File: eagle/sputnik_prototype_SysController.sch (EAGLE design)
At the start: 50 parts, among them U1 MEGA128-M, Y2 8MHZ

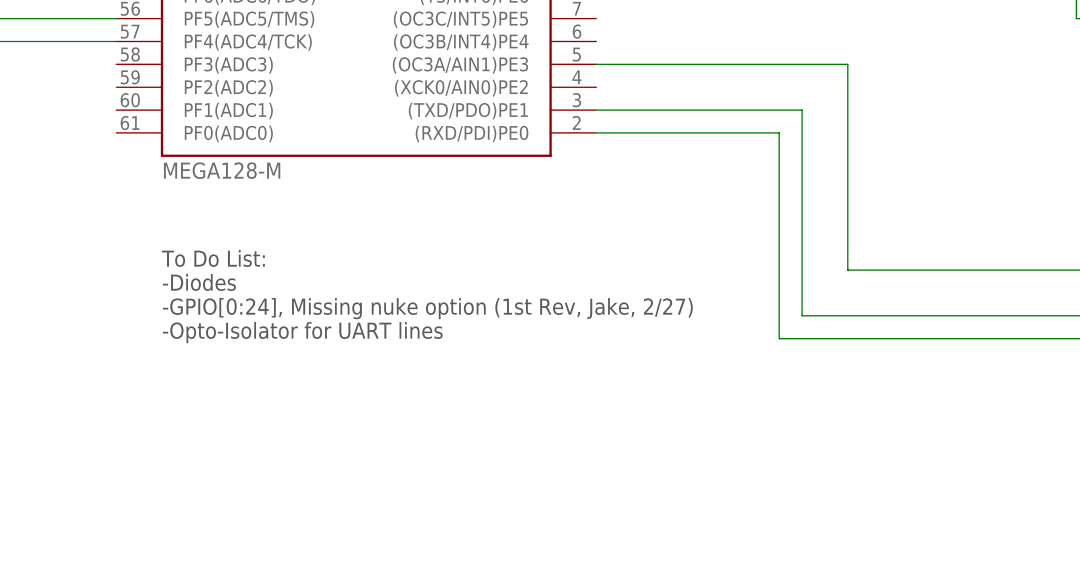
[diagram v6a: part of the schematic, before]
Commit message: Updated to do lists
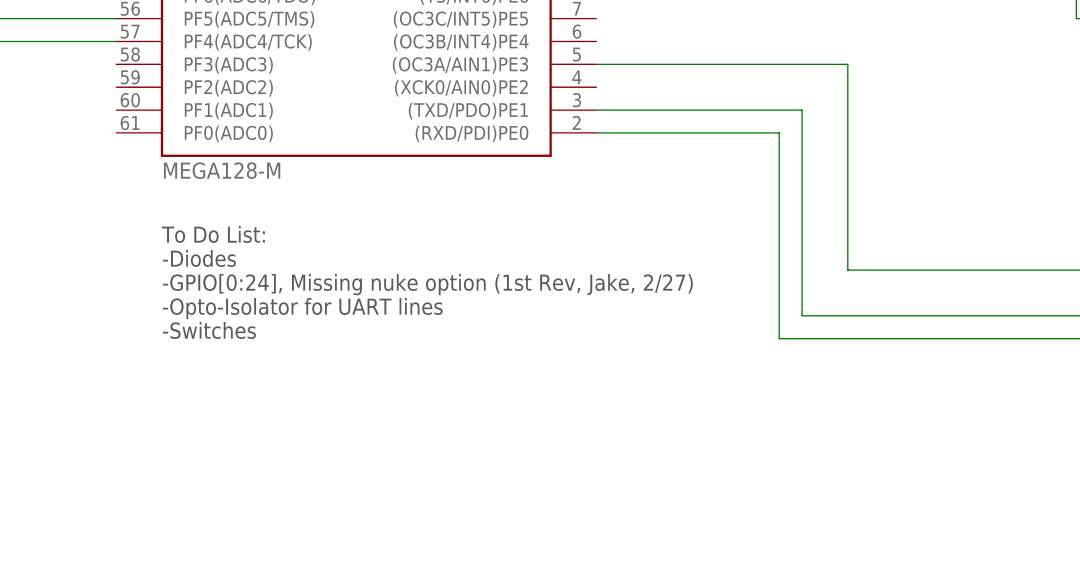
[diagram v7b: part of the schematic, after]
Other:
- note added: "To Do List: -Diodes -GPIO[0:24], Missing nuke option (1st Rev, Jake, 2/27) -Opto-Isolator for UART lines -Switches"
- note removed: "To Do List: -Diodes -GPIO[0:24], Missing nuke option (1st Rev, Jake, 2/27) -Opto-Isolator for UART lines"
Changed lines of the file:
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@@
 -Diodes
 -GPIO[0:24], Missing nuke option (1st Rev, Jake, 2/27)
--Opto-Isolator for UART lines</text>
+-Opto-Isolator for UART lines
+-Switches</text>
 <text x="431.8" y="287.02" size="1.778" layer="97">GPIO</text>
 <text x="431.8" y="248.92" size="1.778" layer="97">GPIO</text>

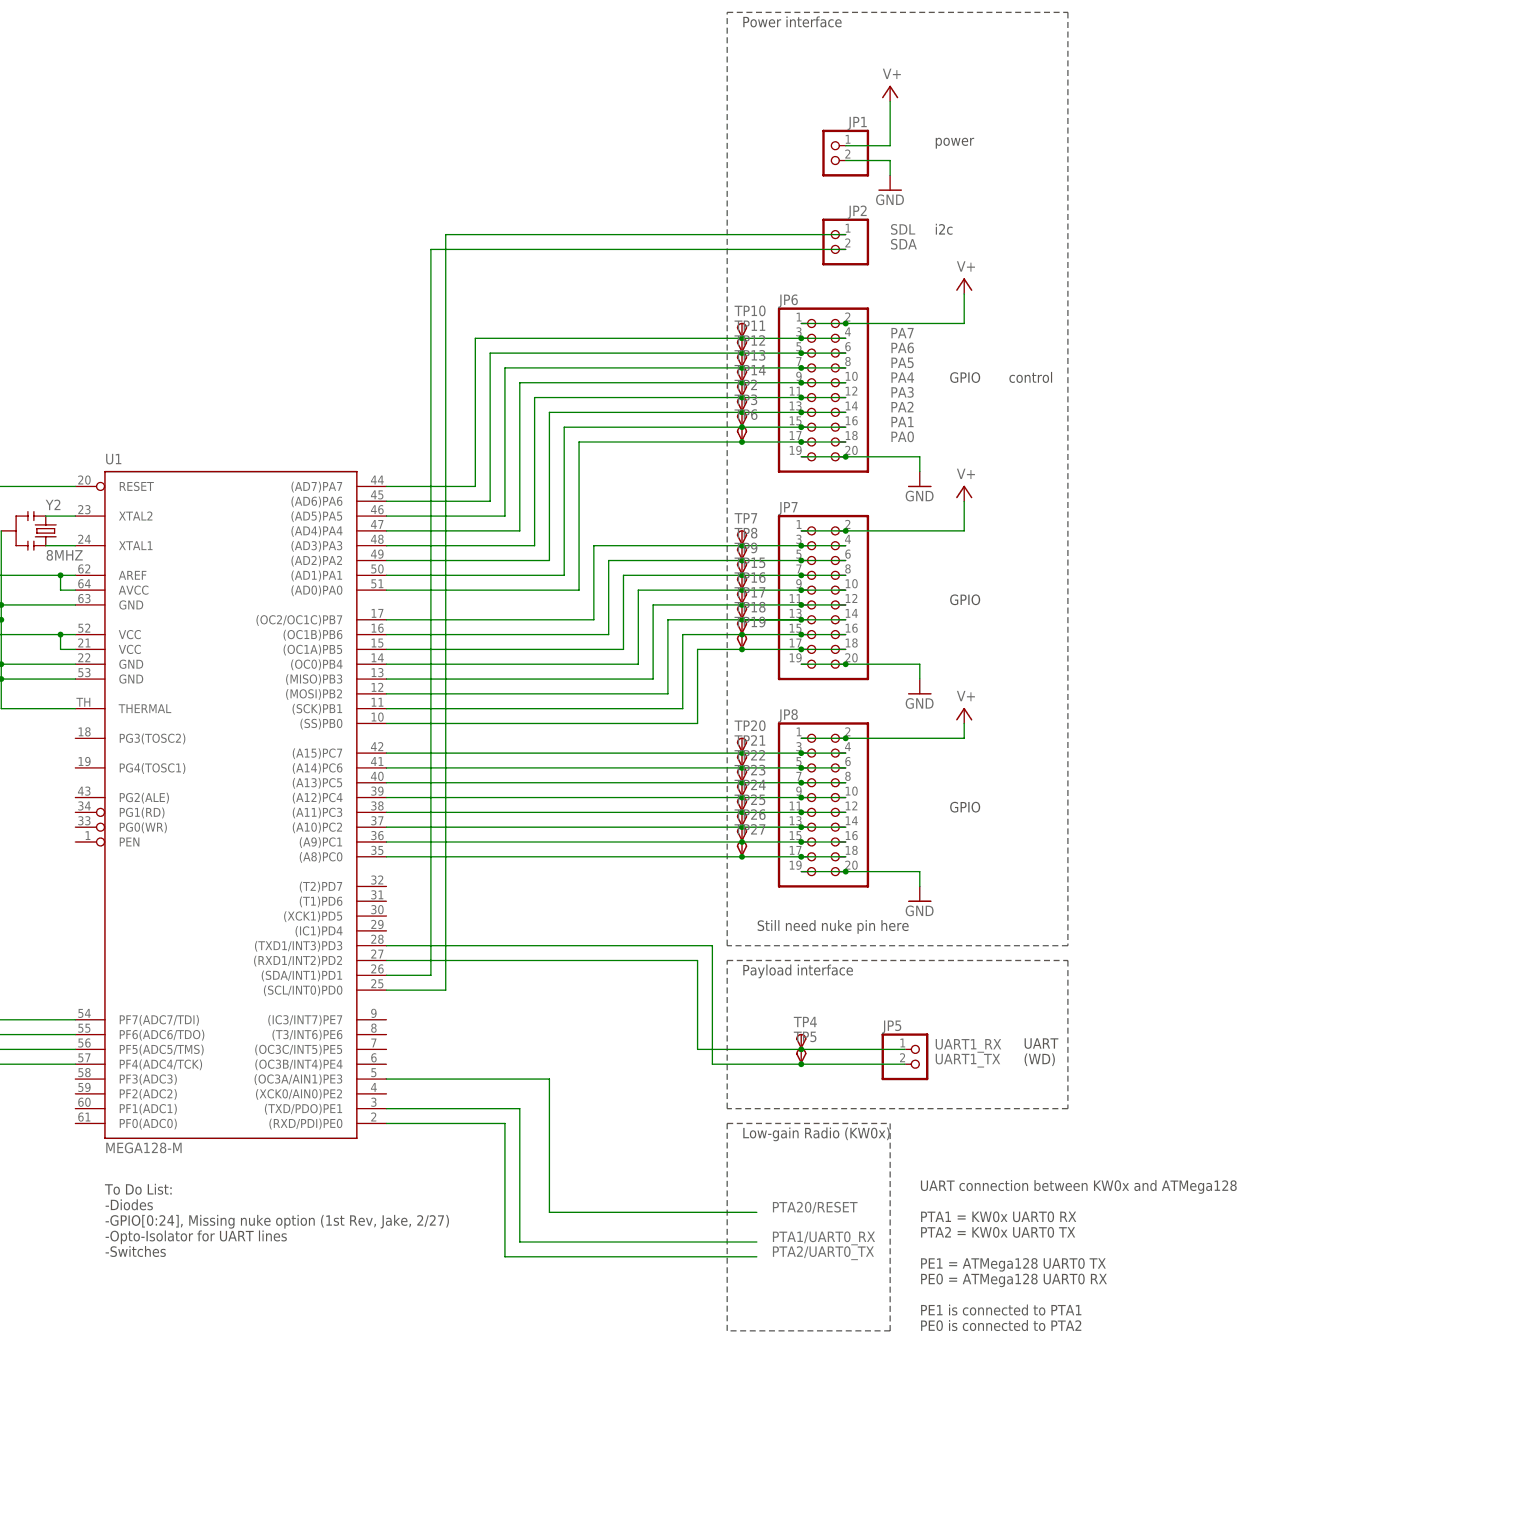
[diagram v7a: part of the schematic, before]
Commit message: Added optocoupler datasheet and into the schematic
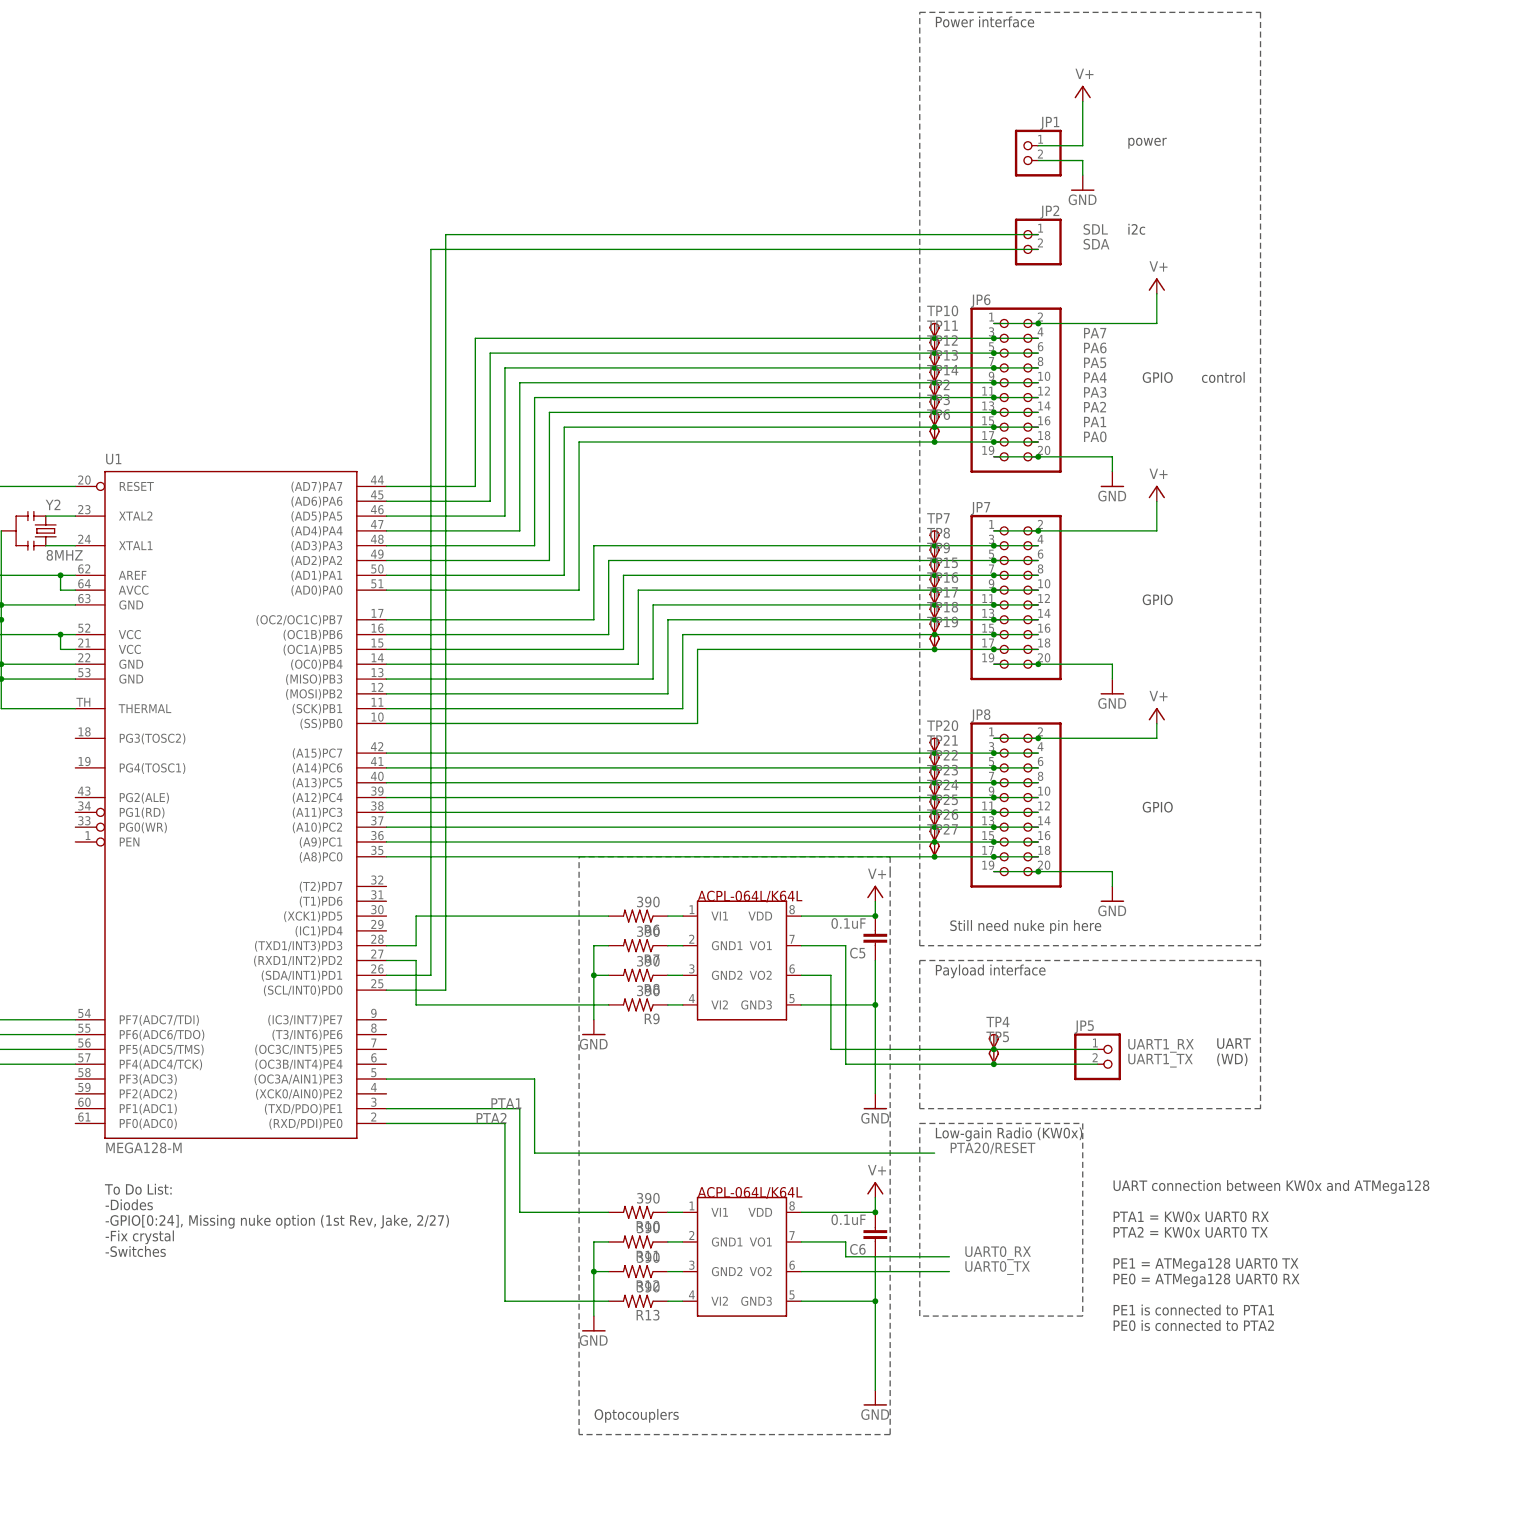
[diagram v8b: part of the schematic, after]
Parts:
- added C5, C6: 0.1uF, rcl_custom:C-EU0603-B-NOSILK
- added R10, R11, R12, R13, R6, R7, R8, R9: 390, rcl_custom:R-US_0603-B-NOSILK
- added U$2, U$3: ACPL-064L/K64L, psas_c3_team05:ACPL-064L/K64L
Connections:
- removed net PTA1/UART0_RX: U1.(TXD/PDO)PE1
- removed net PTA2/UART0_TX: U1.(RXD/PDI)PE0
- new net N$10: R6.2, U1.(TXD1/INT3)PD3
- new net N$16: R9.2, U1.(RXD1/INT2)PD2
- new net N$18: R6.1, U$2.VI1
- new net N$19: R7.1, U$2.GND1
- new net N$20: R8.1, U$2.GND2
- new net N$21: R9.1, U$2.VI2
- new net N$26: R10.1, U$3.VI1
- new net N$27: R11.1, U$3.GND1
- new net N$28: R12.1, U$3.GND2
- new net N$29: R13.1, U$3.VI2
- new net PTA1: R10.2, U1.(TXD/PDO)PE1
- new net PTA2: R13.2, U1.(RXD/PDI)PE0
- new net UART0_RX: U$3.VO1
- new net UART0_TX: U$3.VO2
- net GND: now also C5.1, C6.1, R11.2, R12.2, R7.2, R8.2, U$2.GND3, U$3.GND3
- net UART1_RX: now also U$2.VO2; no longer U1.(RXD1/INT2)PD2
- net UART1_TX: now also U$2.VO1; no longer U1.(TXD1/INT3)PD3
- net V+: now also C5.2, C6.2, U$2.VDD, U$3.VDD
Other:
- note added: "Optocouplers"
- note added: "To Do List: -Diodes -GPIO[0:24], Missing nuke option (1st Rev, Jake, 2/27) -Fix crystal -Switches"
- note removed: "To Do List: -Diodes -GPIO[0:24], Missing nuke option (1st Rev, Jake, 2/27) -Opto-Isolator for UART lines -Switches"
- moved on the sheet: JP1, JP2, JP5, JP6, JP7, JP8, TP10, TP11, TP12, TP13, TP14, TP15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
